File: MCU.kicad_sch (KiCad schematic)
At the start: 106 parts, among them J1 FTDI, J10 mist, J12 Water_Level, J13 Main_Input_Jack, J14 Battery, J15 Display, J16 Rotary encoder, J17 Temp, J18 Temp2, J19 Water_Pump, J2 LED, J20 Conn_01x04_Socket, J3 C8465, J4 C8465, J6 C8465, J8 Fan_Exhaust, J9 Fan_Continous, K1 G5NB-1A-E DC12, Q10 AO3406, Q2 AO3406, Q3 AO3406, Q4 AO3406, Q5 AO3406, Q6 AO3406, Q7 SI2301, Q8 AO3406, Q9 AO3406, SW1 SW_Omron_B3FS, SW2 SW_Omron_B3FS, U1 TPS63070RNMR, U2 ESP32-WROOM-32, U3 AMS1117-5.0, U5 PCF8574, U6 MAX17048G_T10, U7 TP4056, U8 DS1307+, U9 G5NB-1A-E DC12, Y1 32.768kHz Quartz Crystal

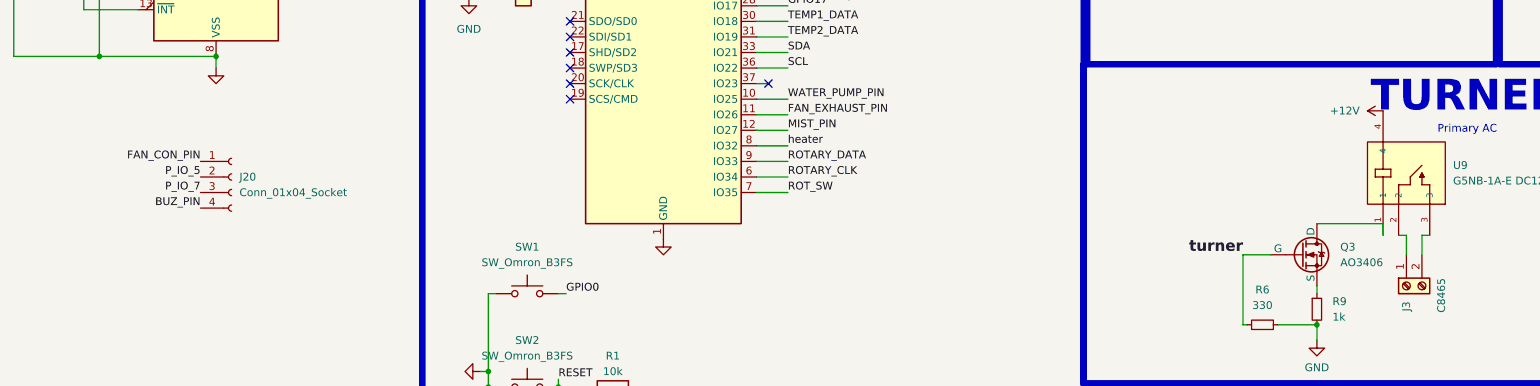
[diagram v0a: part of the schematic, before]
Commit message: changed picture in readme
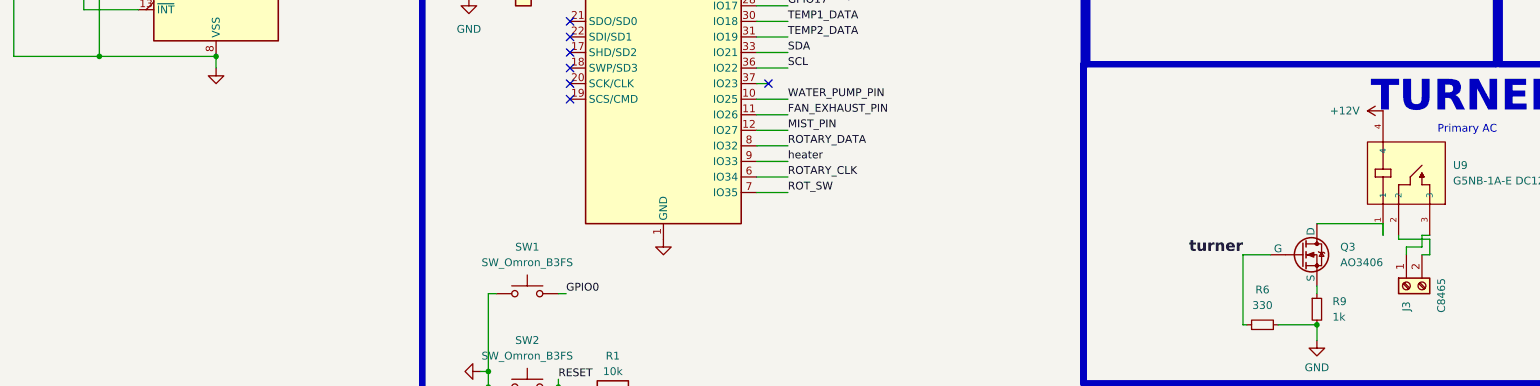
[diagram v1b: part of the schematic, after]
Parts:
- removed J20: Conn_01x04_Socket, Connector_JST:JST_GH_SM04B-GHS-TB_1x04-1MP_P1.25mm_Horizontal, symbol Connector:Conn_01x04_Socket
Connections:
- net ROTARY_DATA: now also U2.8 (IO32); no longer U2.9 (IO33)
- net heater: now also U2.9 (IO33); no longer U2.8 (IO32)
- net at J3.1 (Pin_1): now also U9.3; no longer U9.2
- net at J3.2 (Pin_2): now also U9.2; no longer U9.3
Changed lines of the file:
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@@
 	(wire
 		(pts
-			(xy 340.36 129.54) (xy 340.36 126.365)
-		)
-		(stroke
-			(width 0)
-			(type default)
-		)
-	)
-	(wire
-		(pts
 			(xy 287.02 200.66) (xy 294.005 200.66)
 		)
@@
 	(wire
 		(pts
-			(xy 231.775 111.76) (xy 236.855 111.76)
+			(xy 409.575 46.355) (xy 431.8 46.355)
 		)
 		(stroke
@@
 	(wire
 		(pts
-			(xy 409.575 46.355) (xy 431.8 46.355)
+			(xy 318.77 46.355) (xy 318.77 57.785)
 		)
 		(stroke
@@
 	(wire
 		(pts
-			(xy 318.77 46.355) (xy 318.77 57.785)
+			(xy 508 73.025) (xy 525.78 73.025)
 		)
 		(stroke
@@
 	(wire
 		(pts
-			(xy 508 73.025) (xy 525.78 73.025)
+			(xy 189.865 269.875) (xy 197.485 269.875)
 		)
 		(stroke
@@
 	(wire
 		(pts
-			(xy 189.865 269.875) (xy 197.485 269.875)
+			(xy 231.775 264.795) (xy 235.585 264.795)
 		)
 		(stroke
@@
 	(wire
 		(pts
-			(xy 231.775 264.795) (xy 235.585 264.795)
+			(xy 197.485 270.51) (xy 197.485 269.875)
 		)
 		(stroke
@@
 	(wire
 		(pts
-			(xy 197.485 270.51) (xy 197.485 269.875)
+			(xy 252.095 262.255) (xy 258.445 262.255)
 		)
 		(stroke
@@
 	(wire
 		(pts
-			(xy 252.095 262.255) (xy 258.445 262.255)
+			(xy 341.63 129.54) (xy 340.36 129.54)
 		)
 		(stroke
@@
 	(wire
 		(pts
+			(xy 340.36 128.27) (xy 337.82 128.27)
+		)
+		(stroke
+			(width 0)
+			(type default)
+		)
+	)
+	(wire
+		(pts
 			(xy 331.47 193.04) (xy 329.565 193.04)
 		)
@@
 	(wire
 		(pts
+			(xy 336.55 127) (xy 336.55 126.365)
+		)
+		(stroke
+			(width 0)
+			(type default)
+		)
+	)
+	(wire
+		(pts
 			(xy 143.51 97.155) (xy 124.46 97.155)
 		)
@@
 	(wire
 		(pts
+			(xy 231.775 114.3) (xy 236.855 114.3)
+		)
+		(stroke
+			(width 0)
+			(type default)
+		)
+	)
+	(wire
+		(pts
 			(xy 205.105 267.335) (xy 205.105 269.875)
 		)
@@
 	(wire
 		(pts
-			(xy 337.82 129.54) (xy 337.82 126.365)
-		)
-		(stroke
-			(width 0)
-			(type default)
-		)
-	)
-	(wire
-		(pts
 			(xy 34.29 210.82) (xy 34.29 209.55)
 		)
@@
 	(wire
 		(pts
+			(xy 336.55 127) (xy 341.63 127)
+		)
+		(stroke
+			(width 0)
+			(type default)
+		)
+	)
+	(wire
+		(pts
 			(xy 509.27 129.54) (xy 509.27 128.27)
 		)
@@
 	(wire
 		(pts
+			(xy 231.775 111.76) (xy 236.855 111.76)
+		)
+		(stroke
+			(width 0)
+			(type default)
+		)
+	)
+	(wire
+		(pts
 			(xy 58.42 90.805) (xy 81.28 90.805)
 		)
@@
 	(wire
 		(pts
-			(xy 337.82 126.365) (xy 336.55 126.365)
+			(xy 231.775 91.44) (xy 236.855 91.44)
 		)
 		(stroke
@@
 	(wire
 		(pts
-			(xy 231.775 91.44) (xy 236.855 91.44)
+			(xy 531.495 56.515) (xy 531.495 53.975)
 		)
 		(stroke
@@
 	(wire
 		(pts
-			(xy 531.495 56.515) (xy 531.495 53.975)
+			(xy 266.065 254.635) (xy 269.875 254.635)
 		)
 		(stroke
@@
 	(wire
 		(pts
-			(xy 266.065 254.635) (xy 269.875 254.635)
+			(xy 455.295 134.62) (xy 447.04 134.62)
 		)
 		(stroke
@@
 	(wire
 		(pts
-			(xy 455.295 134.62) (xy 447.04 134.62)
+			(xy 231.775 60.96) (xy 234.95 60.96)
 		)
 		(stroke
@@
 	(wire
 		(pts
-			(xy 231.775 60.96) (xy 234.95 60.96)
+			(xy 431.8 46.355) (xy 431.8 48.895)
 		)
 		(stroke
@@
 	(wire
 		(pts
-			(xy 431.8 46.355) (xy 431.8 48.895)
+			(xy 506.73 141.605) (xy 523.875 141.605)
 		)
 		(stroke
@@
 	(wire
 		(pts
-			(xy 506.73 141.605) (xy 523.875 141.605)
+			(xy 337.82 128.27) (xy 337.82 129.54)
 		)
 		(stroke
@@
 	(wire
 		(pts
-			(xy 198.12 195.58) (xy 208.28 195.58)
+			(xy 340.36 128.27) (xy 340.36 126.365)
 		)
 		(stroke
@@
 	(wire
 		(pts
-			(xy 300.355 52.07) (xy 300.355 63.5)
+			(xy 198.12 195.58) (xy 208.28 195.58)
 		)
 		(stroke
@@
 	(wire
 		(pts
-			(xy 313.055 24.765) (xy 313.055 26.035)
+			(xy 300.355 52.07) (xy 300.355 63.5)
 		)
 		(stroke
@@
 	(wire
 		(pts
-			(xy 231.775 114.3) (xy 236.855 114.3)
+			(xy 313.055 24.765) (xy 313.055 26.035)
 		)
 		(stroke
@@
 	(wire
 		(pts
+			(xy 341.63 127) (xy 341.63 129.54)
+		)
+		(stroke
+			(width 0)
+			(type default)
+		)
+	)
+	(wire
+		(pts
 			(xy 331.47 190.5) (xy 329.565 190.5)
 		)
@@
 	)
 	(label "ROTARY_DATA"
-		(at 236.855 114.3 0)
+		(at 236.855 111.76 0)
 		(fields_autoplaced yes)
 		(effects
@@
 		)
 	)
-	(label "P_IO_5"
-		(at 140.97 116.84 180)
-		(fields_autoplaced yes)
-		(effects
-			(font
-				(size 1.27 1.27)
-			)
-			(justify right bottom)
-		)
-	)
 	(label "SDA"
 		(at 127 71.755 0)
@@
 		)
 	)
-	(label "FAN_CON_PIN"
-		(at 140.97 114.3 180)
-		(fields_autoplaced yes)
-		(effects
-			(font
-				(size 1.27 1.27)
-			)
-			(justify right bottom)
-		)
-	)
 	(label "TPS_PGND"
 		(at 182.88 213.36 0)
@@
 	)
 	(label "heater"
-		(at 236.855 111.76 0)
+		(at 236.855 114.3 0)
 		(fields_autoplaced yes)
 		(effects
@@
 		)
 	)
-	(label "P_IO_7"
-		(at 140.97 119.38 180)
-		(fields_autoplaced yes)
-		(effects
-			(font
-				(size 1.27 1.27)
-			)
-			(justify right bottom)
-		)
-	)
 	(label "SDA"
 		(at 236.855 96.52 0)
@@
 		)
 	)
-	(label "BUZ_PIN"
-		(at 140.97 121.92 180)
-		(fields_autoplaced yes)
-		(effects
-			(font
-				(face "KiCad Font")
-				(size 1.27 1.27)
-			)
-			(justify right bottom)
-		)
-	)
 	(label "SCL"
 		(at 161.29 252.73 90)
@@
 					(unit 1)
 				)
-			)
-		)
-	)
-	(symbol
-		(lib_id "Connector:Conn_01x04_Socket")
-		(at 146.05 116.84 0)
-		(unit 1)
-		(exclude_from_sim no)
-		(in_bom yes)
-		(on_board yes)
-		(dnp no)
-		(fields_autoplaced yes)
-		(property "Reference" "J20"
-			(at 147.32 116.84 0)
-			(effects
-				(font
-					(size 1.27 1.27)
-				)
-				(justify left)
-			)
-		)
-		(property "Value" "Conn_01x04_Socket"
-			(at 147.32 119.38 0)
-			(effects
-				(font
-					(size 1.27 1.27)
-				)
-				(justify left)
-			)
-		)
-		(property "Footprint" "Connector_JST:JST_GH_SM04B-GHS-TB_1x04-1MP_P1.25mm_Horizontal"
-			(at 146.05 116.84 0)
-			(effects
-				(font
-					(size 1.27 1.27)
-				)
-				(hide yes)
-			)
-		)
-		(property "Datasheet" "~"
-			(at 146.05 116.84 0)
-			(effects
-				(font
-					(size 1.27 1.27)
-				)
-				(hide yes)
-			)
-		)
-		(property "Description" ""
-			(at 146.05 116.84 0)
-			(effects
-				(font
-					(size 1.27 1.27)
-				)
-				(hide yes)
-			)
-		)
-		(pin "1"
-		)
-		(pin "2"
-		)
-		(pin "3"
-		)
-		(pin "4"
-		)
-		(instances
-			(project "Capibator_PCB"
-				(path "/314af396-fc31-4fe3-9f85-bbd0c4bf0b50/6d26da2f-4df7-46b4-abe0-c85ffa1a5908"
-					(reference "J20")
-					(unit 1)
-				)

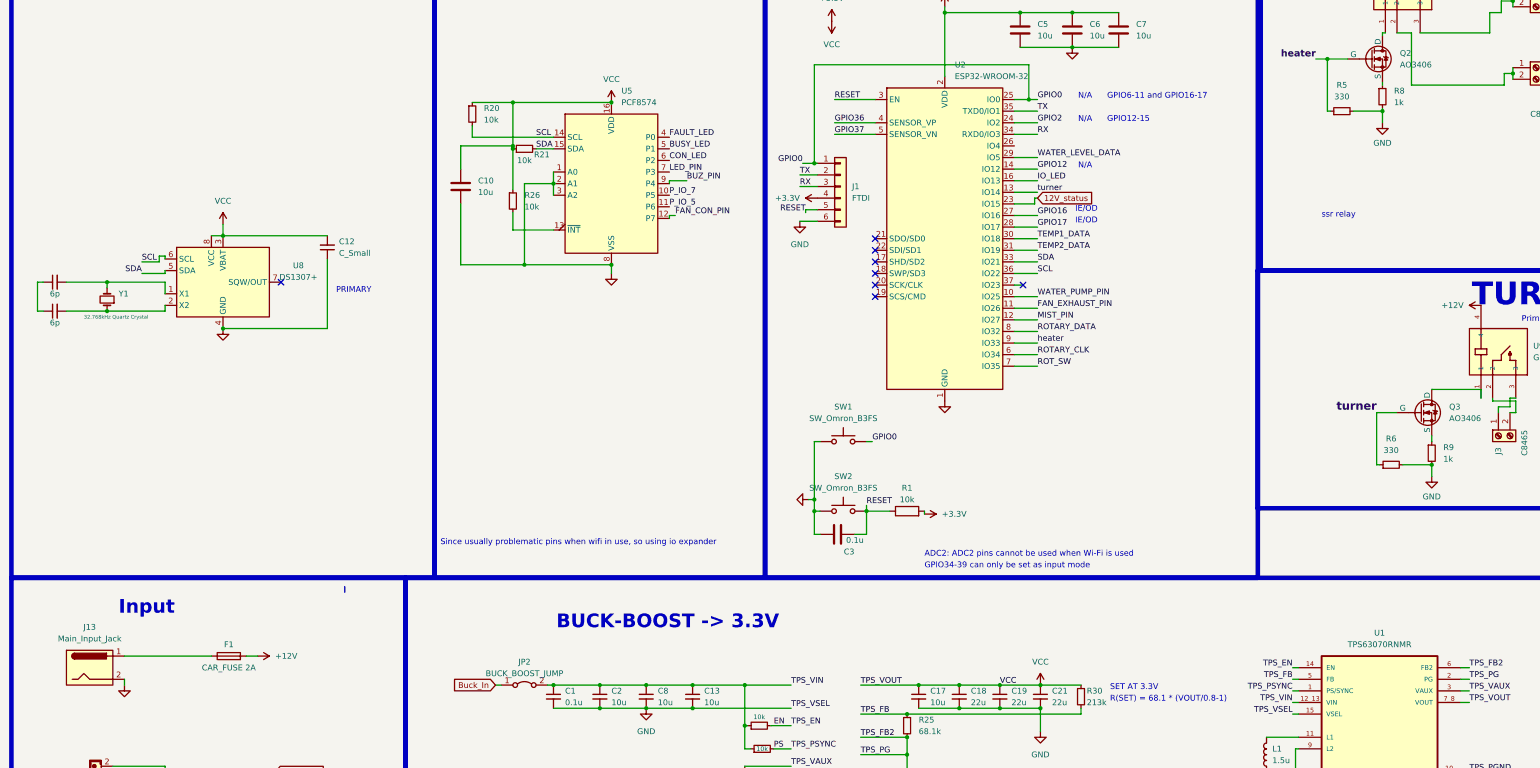
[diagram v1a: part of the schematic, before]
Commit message: generated bom for jlcpcb
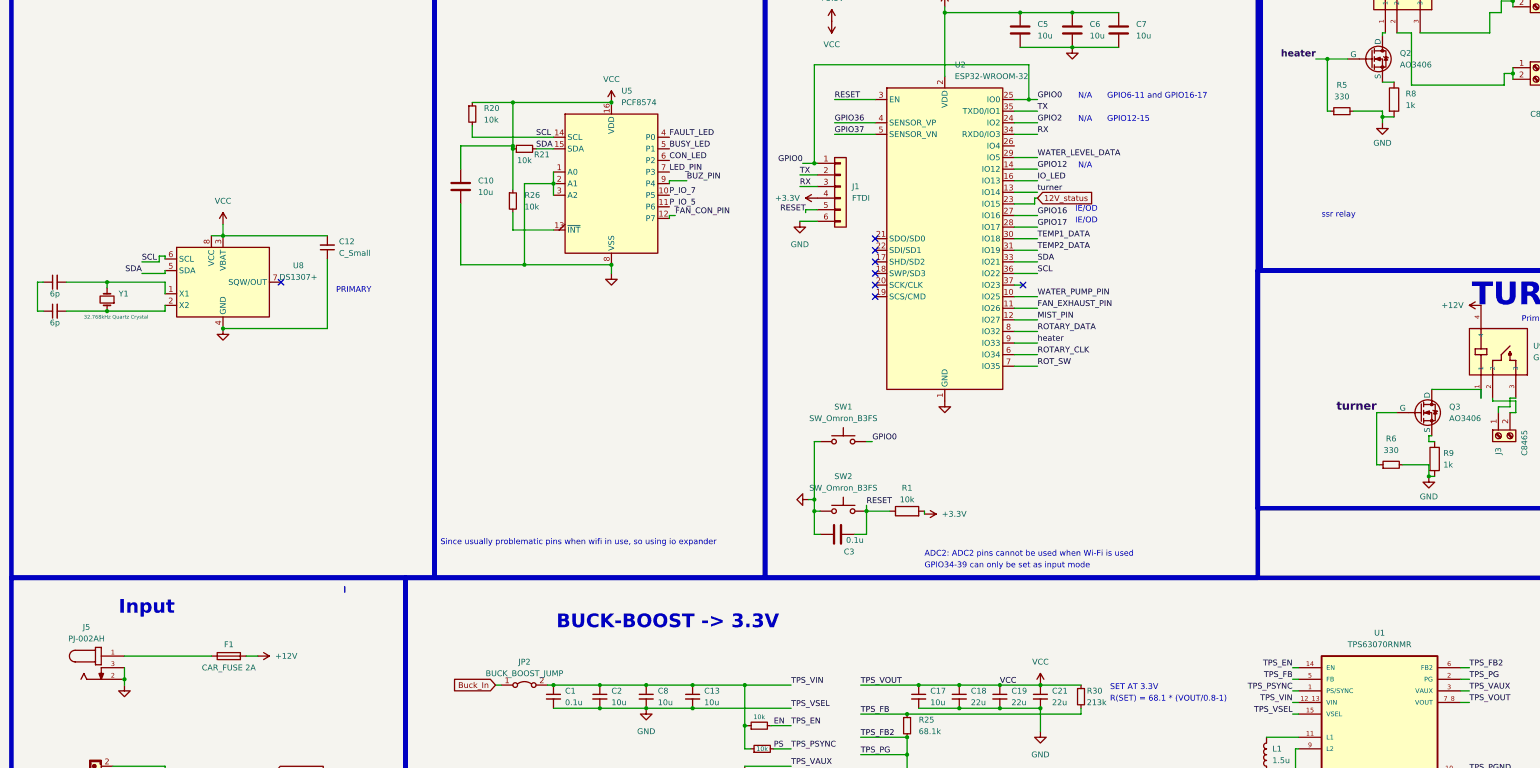
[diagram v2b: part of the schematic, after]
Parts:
- removed J13: Main_Input_Jack, Connector_BarrelJack:BarrelJack_CLIFF_FC681465S_SMT_Horizontal, symbol Connector:Jack-DC
- added J5: PJ-002AH, PJ-002AH:CUI_PJ-002AH, symbol dc-jack:PJ-002AH
- J15: footprint Connector_JST:JST_GH_SM04B-GHS-TB_1x04-1MP_P1.25mm_Horizontal -> Connector_JST:JST_GH_BM04B-GHS-TBT_1x04-1MP_P1.25mm_Vertical
- J16: footprint Connector_JST:JST_GH_SM05B-GHS-TB_1x05-1MP_P1.25mm_Horizontal -> Connector_JST:JST_GH_BM05B-GHS-TBT_1x05-1MP_P1.25mm_Vertical
- L1: footprint Inductor_SMD:L_6.3x6.3_H3 -> Inductor_SMD:L_0805_2012Metric
- R8, R9: symbol Device:R_Small -> Device:R
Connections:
- net GND: now also J5.2, J5.3
- net at F1.1: now also J5.1
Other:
- moved on the sheet: R8, R9

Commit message: corrected few  mistakes, generated correct bom  with lcsc part numbers
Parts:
- removed F1: CAR_FUSE 2A, Fuse:Fuse_1206_3216Metric, symbol Device:Fuse
- added J5, J7: C8465, TerminalBlock:TerminalBlock_Altech_AK300-2_P5.00mm, symbol Connector:Screw_Terminal_01x02
- added R2: 3k, Resistor_SMD:R_0805_2012Metric, symbol Device:R_Small
- C12: value C_Small -> 10u
- D1: footprint Diode_SMD:D_0805_2012Metric -> Diode_SMD:D_SOD-323F
- D10, D11, D3, D6, D8: footprint Diode_SMD:D_0805_2012Metric -> Diode_SMD:D_SOD-123F
- L1: footprint Inductor_SMD:L_0805_2012Metric -> Inductor_SMD:L_Murata_LQH2MCNxxxx02_2.0x1.6mm
- R11, R12, R14, R15, R37: value 1K -> 100
- R30: value 213k -> 210k
- R31, R32: value 1.5k -> 100
- R36: footprint Resistor_SMD:R_0805_2012Metric -> Diode_SMD:D_SOD-123F
- R5, R6: value 330 -> 100
- Y1: footprint Crystal:Crystal_SMD_3215-2Pin_3.2x1.5mm -> Crystal:Crystal_SMD_2012-2Pin_2.0x1.2mm_HandSoldering
- renumbered J5 to J20
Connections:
- net +12V: now also J20.1
- net TPS_FB: now also R2.1; no longer R30.2
- net at J4.1 (Pin_1), J4.2 (Pin_2), K1.2: now also J7.1 (Pin_1), J7.2 (Pin_2)
- net at J6.1 (Pin_1), J6.2 (Pin_2), K1.3: now also J5.1 (Pin_1), J5.2 (Pin_2)
- new net: R2.2, R30.2
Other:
- moved on the sheet: J4, J6

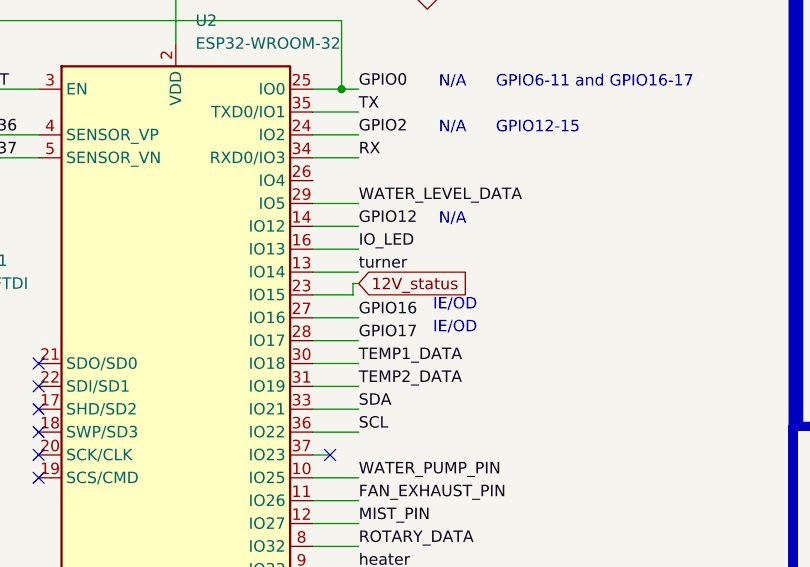
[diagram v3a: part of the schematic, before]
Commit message: cleaned up tracks, added teardrops, copper fill and improved spacing
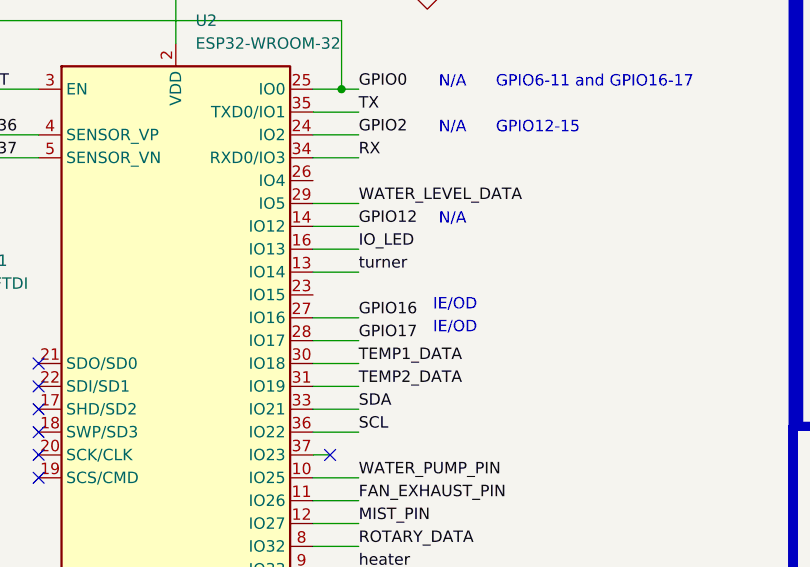
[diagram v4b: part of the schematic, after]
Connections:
- net 12V_status: no longer names the net of U2.23 (IO15)
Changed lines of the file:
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@@
 	(wire
 		(pts
-			(xy 236.22 83.82) (xy 231.775 83.82)
-		)
-		(stroke
-			(width 0)
-			(type default)
-		)
-	)
-	(wire
-		(pts
 			(xy 36.83 182.88) (xy 66.04 182.88)
 		)
@@
 	(wire
 		(pts
-			(xy 236.22 82.55) (xy 236.855 82.55)
-		)
-		(stroke
-			(width 0)
-			(type default)
-		)
-	)
-	(wire
-		(pts
 			(xy 121.92 61.595) (xy 121.92 71.12)
 		)
@@
 	(wire
 		(pts
-			(xy 236.22 82.55) (xy 236.22 83.82)
-		)
-		(stroke
-			(width 0)
-			(type default)
-		)
-	)
-	(wire
-		(pts
 			(xy 499.745 128.905) (xy 499.745 131.445)
 		)
@@
 		)
 	)
-	(global_label "12V_status"
-		(shape input)
-		(at 236.855 82.55 0)
-		(fields_autoplaced yes)
-		(effects
-			(font
-				(size 1.27 1.27)
-			)
-			(justify left)
-		)
-		(property "Intersheetrefs" "${INTERSHEET_REFS}"
-			(at 250.121 82.55 0)
-			(effects
-				(font
-					(size 1.27 1.27)
-				)
-				(justify left)
-				(hide yes)
-			)
-		)
-	)
